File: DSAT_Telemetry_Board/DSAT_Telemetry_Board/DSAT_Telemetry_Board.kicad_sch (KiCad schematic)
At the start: 1 part

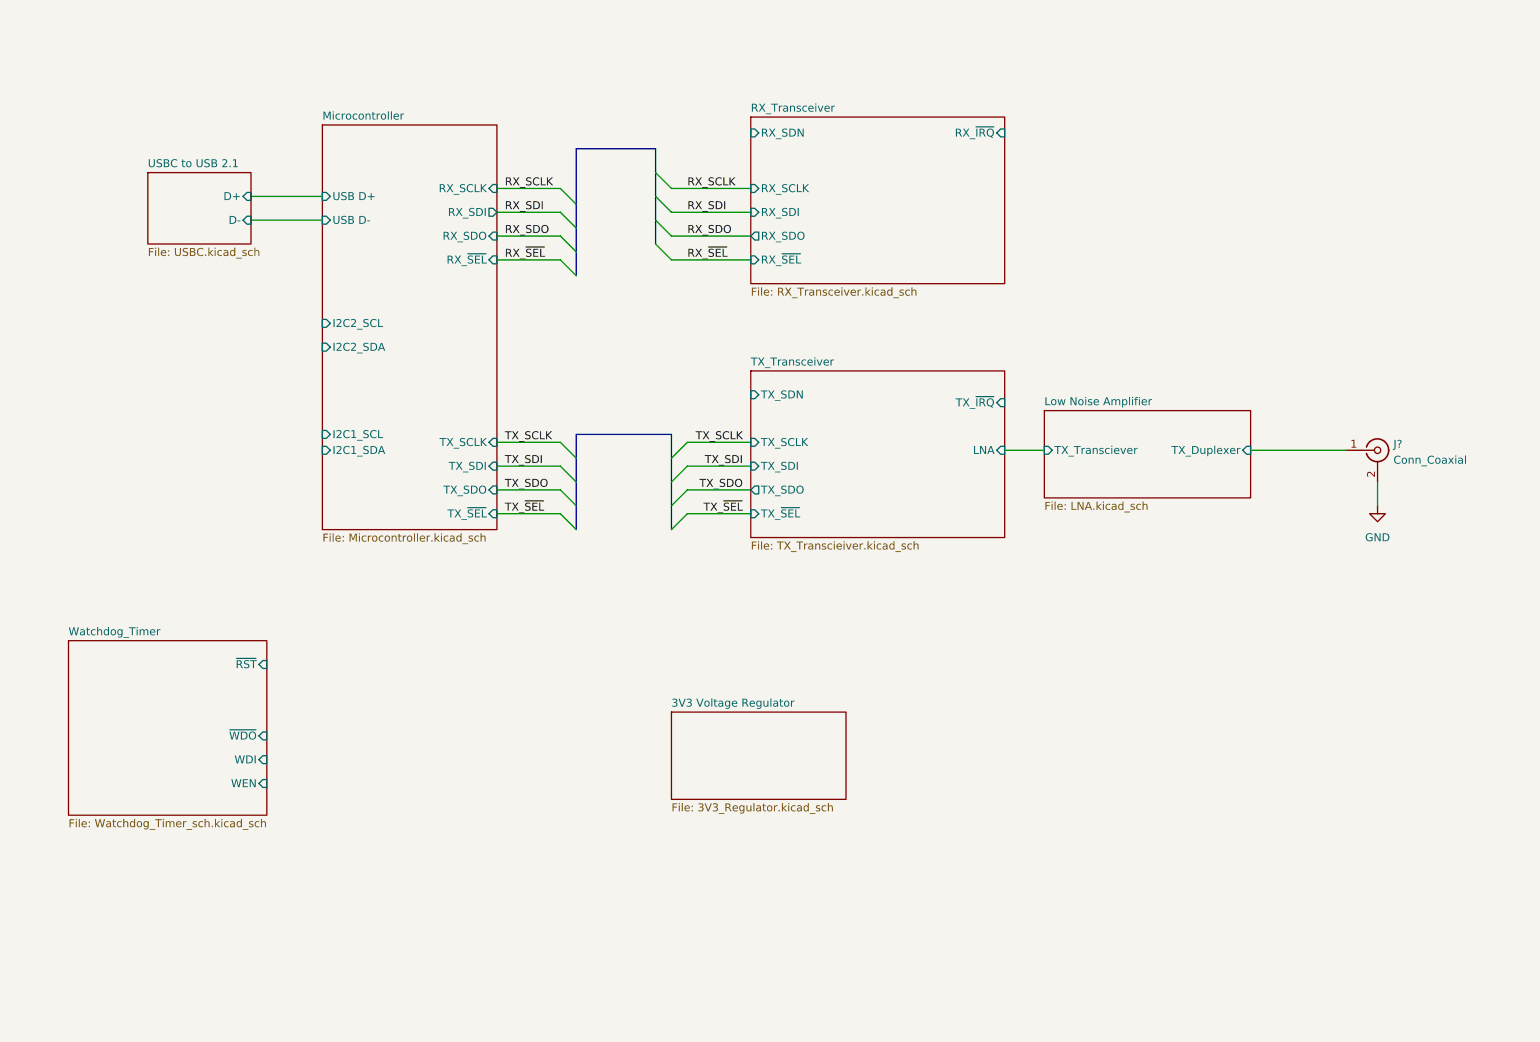
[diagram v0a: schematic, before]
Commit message: RX_SWitch, test points
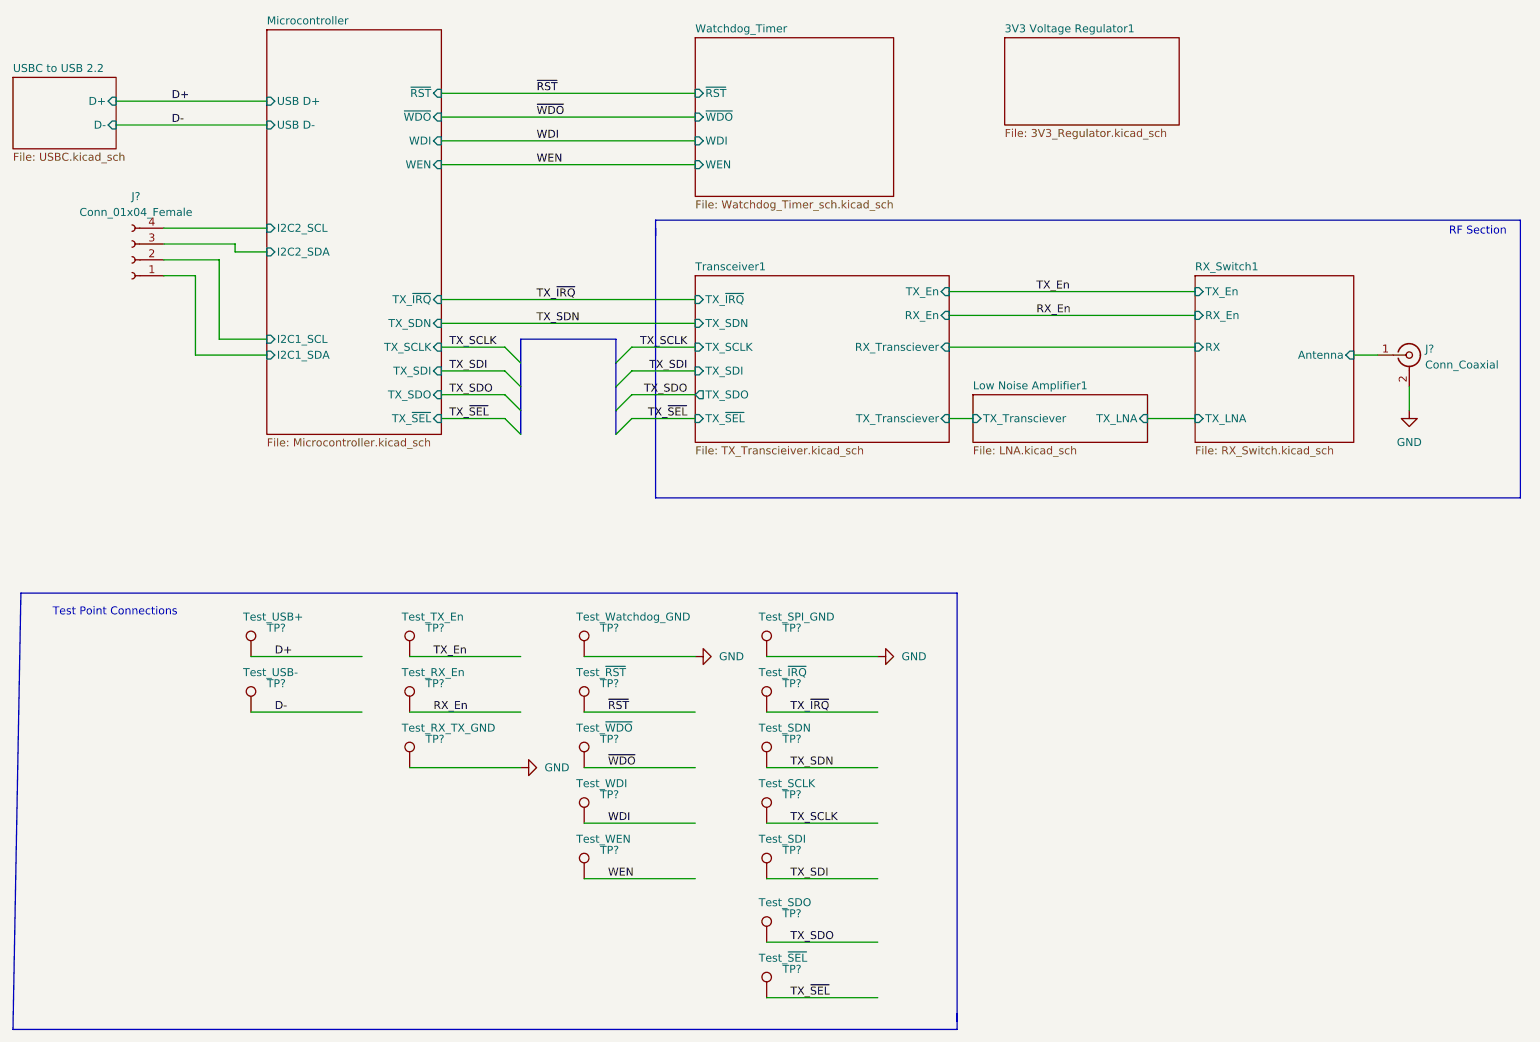
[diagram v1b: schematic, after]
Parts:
- removed J?: Conn_Coaxial, symbol Connector:Conn_Coaxial
- added J?: Conn_Coaxial, symbol Connector:Conn_Coaxial
- added J?: Conn_01x04_Female, Connector_PinHeader_2.54mm:PinHeader_1x04_P2.54mm_Vertical, symbol Connector:Conn_01x04_Female
- added TP?: Test_~{RST}, TestPoint:TestPoint_Pad_D2.5mm, symbol Connector:TestPoint
- added TP?: Test_TX_En, TestPoint:TestPoint_Pad_D2.5mm, symbol Connector:TestPoint
- added TP?: Test_RX_TX_GND, TestPoint:TestPoint_Pad_D2.5mm, symbol Connector:TestPoint
- added TP?: Test_WDI, TestPoint:TestPoint_Pad_D2.5mm, symbol Connector:TestPoint
- added TP?: Test_USB-, TestPoint:TestPoint_Pad_D2.5mm, symbol Connector:TestPoint
- added TP?: Test_~{SEL}, TestPoint:TestPoint_Pad_D2.5mm, symbol Connector:TestPoint
- added TP?: Test_SDN, TestPoint:TestPoint_Pad_D2.5mm, symbol Connector:TestPoint
- added TP?: Test_SDO, TestPoint:TestPoint_Pad_D2.5mm, symbol Connector:TestPoint
- added TP?: Test_SDI, TestPoint:TestPoint_Pad_D2.5mm, symbol Connector:TestPoint
- added TP?: Test_USB+, TestPoint:TestPoint_Pad_D2.5mm, symbol Connector:TestPoint
- added TP?: Test_~{WDO}, TestPoint:TestPoint_Pad_D2.5mm, symbol Connector:TestPoint
- added TP?: Test_SPI_GND, TestPoint:TestPoint_Pad_D2.5mm, symbol Connector:TestPoint
- added TP?: Test_~{IRQ}, TestPoint:TestPoint_Pad_D2.5mm, symbol Connector:TestPoint
- added TP?: Test_Watchdog_GND, TestPoint:TestPoint_Pad_D2.5mm, symbol Connector:TestPoint
- added TP?: Test_RX_En, TestPoint:TestPoint_Pad_D2.5mm, symbol Connector:TestPoint
- added TP?: Test_SCLK, TestPoint:TestPoint_Pad_D2.5mm, symbol Connector:TestPoint
- added TP?: Test_WEN, TestPoint:TestPoint_Pad_D2.5mm, symbol Connector:TestPoint
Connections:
- net GND: now also J?.2 (Ext), TP?.1, TP?.1, TP?.1
- net Microcontroller/I2C1_SCL: now also J?.2 (Pin_2)
- net Microcontroller/I2C1_SDA: now also J?.1 (Pin_1)
- net Microcontroller/I2C2_SCL: now also J?.4 (Pin_4)
- net Microcontroller/I2C2_SDA: now also J?.3 (Pin_3)
- net TX_SCLK: now also TP?.1
- net TX_SDI: now also TP?.1
- net TX_SDO: now also TP?.1
- net TX_~{SEL}: now also TP?.1
- new net D+: TP?.1
- new net D-: TP?.1
- new net RX_En: TP?.1
- new net RX_Switch1/Antenna: J?.1 (In)
- new net TX_En: TP?.1
- new net TX_SDN: TP?.1
- new net TX_~{IRQ}: TP?.1
- new net WDI: TP?.1
- new net WEN: TP?.1
- new net ~{RST}: TP?.1
- new net ~{WDO}: TP?.1
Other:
- removed sheet 3V3 Voltage Regulator
- removed sheet Low Noise Amplifier
- removed sheet RX_Transceiver
- removed sheet TX_Transceiver
- removed sheet USBC to USB 2.1
- added sheet 3V3 Voltage Regulator1 (3V3_Regulator.kicad_sch)
- added sheet Low Noise Amplifier1 (LNA.kicad_sch)
- added sheet RX_Switch1 (RX_Switch.kicad_sch)
- added sheet Transceiver1 (TX_Transcieiver.kicad_sch)
- added sheet USBC to USB 2.2 (USBC.kicad_sch)
- sheet Microcontroller ports: added TX_SDN, TX_~{IRQ}, WDI, WEN, ~{RST}, ~{WDO}; removed RX_SCLK, RX_SDI, RX_SDO, RX_~{SEL}
- note added: "RF Section"
- note added: "Test Point Connections"

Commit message: RX_SWitch, test points
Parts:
- J2: renamed from J?; footprint (none) -> Connector_Coaxial:SMA_Amphenol_132134_Vertical
- gave numbers to parts that had none: 18

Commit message: Layout halfway done
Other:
- sheet Microcontroller ports: added USB_D+, USB_D-; removed USB D+, USB D-
- sheet USBC to USB 2.2 ports: added USB_D+, USB_D-; removed D+, D-
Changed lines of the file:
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@@
       (effects (font (size 1.27 1.27)) (justify left top))
     )
-    (pin "D+" input (at 36.83 43.18 0)
-      (effects (font (size 1.27 1.27)) (justify right))
-    )
-    (pin "D-" input (at 36.83 46.99 0)
+    (pin "USB_D+" input (at 36.83 43.18 0)
+      (effects (font (size 1.27 1.27)) (justify right))
+    )
+    (pin "USB_D-" input (at 36.83 46.99 0)
       (effects (font (size 1.27 1.27)) (justify right))
     )
@@
       (effects (font (size 1.27 1.27)) (justify left top))
     )
-    (pin "USB D-" input (at 60.96 46.99 180)
-      (effects (font (size 1.27 1.27)) (justify left))
-    )
-    (pin "USB D+" input (at 60.96 43.18 180)
-      (effects (font (size 1.27 1.27)) (justify left))
-    )
     (pin "I2C2_SCL" input (at 60.96 63.5 180)
       (effects (font (size 1.27 1.27)) (justify left))
@@
     (pin "TX_~{IRQ}" input (at 88.9 74.93 0)
       (effects (font (size 1.27 1.27)) (justify right))
+    )
+    (pin "USB_D+" input (at 60.96 43.18 180)
+      (effects (font (size 1.27 1.27)) (justify left))
+    )
+    (pin "USB_D-" input (at 60.96 46.99 180)
+      (effects (font (size 1.27 1.27)) (justify left))
     )
   )
@@
       (reference "#PWR0145") (unit 1) (value "GND") (footprint "")
     )
-    (path "/20e2c0b4-e001-4da0-871f-4df92a319e8f/3cbded9b-575b-4629-a1c2-e5f5a8f91c4a"
-      (reference "#PWR0146") (unit 1) (value "+3.3V") (footprint "")
+    (path "/20e2c0b4-e001-4da0-871f-4df92a319e8f/7c877262-db40-4149-938f-f47562e71d6d"
+      (reference "#PWR0146") (unit 1) (value "VBUS") (footprint "")
     )
     (path "/199c9d7d-1017-4719-8a87-dec201b08eca/c65dde47-16f3-4852-b566-30a2c9e4d8a5"
